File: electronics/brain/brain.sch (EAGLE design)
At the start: 7 parts

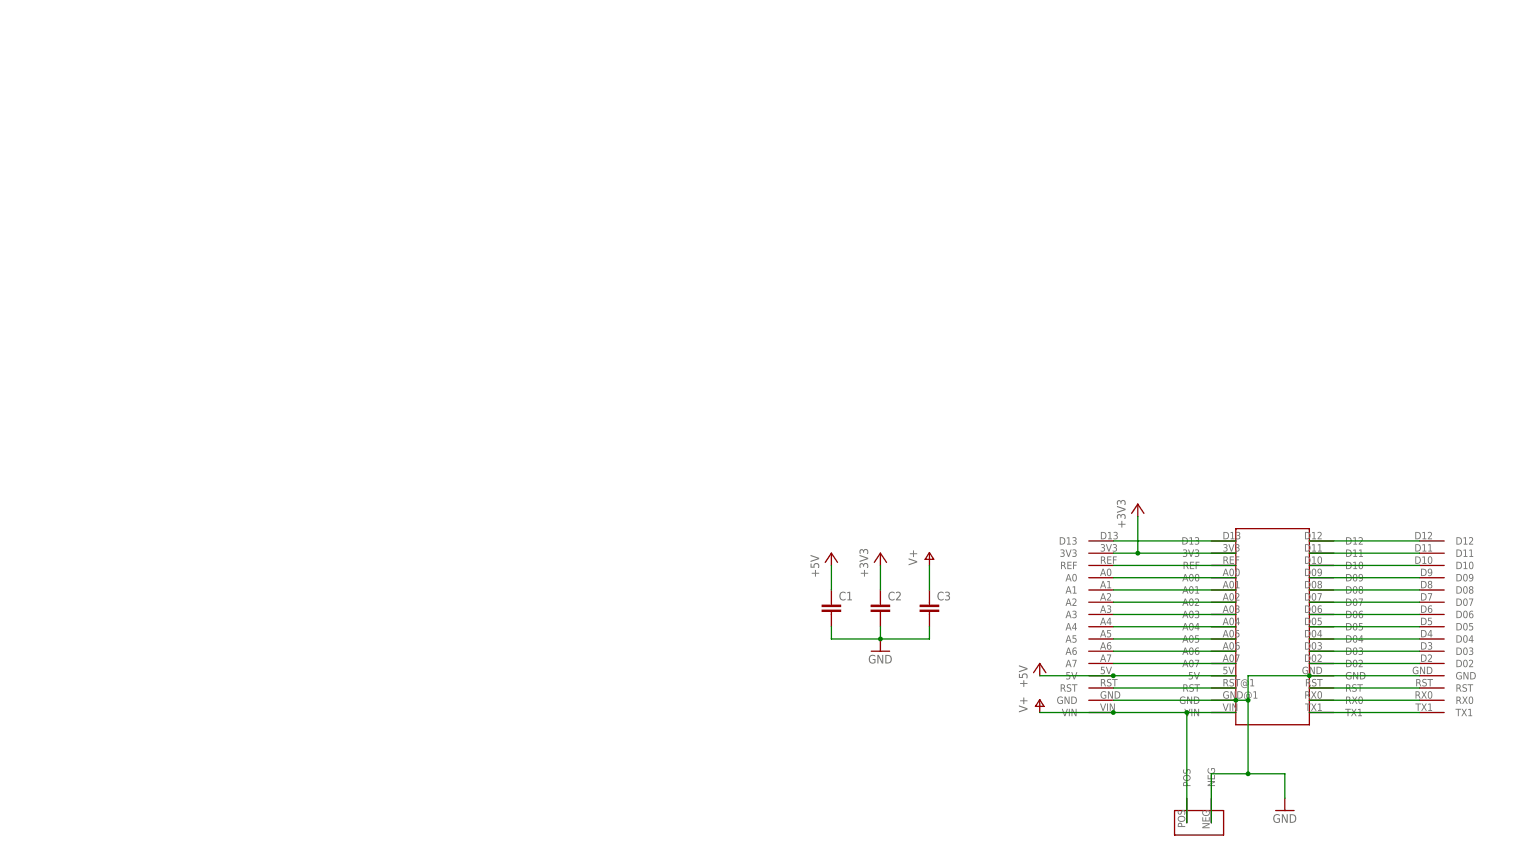
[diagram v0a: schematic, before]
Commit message: Fleshed out pin mapping. Routed new brain board.
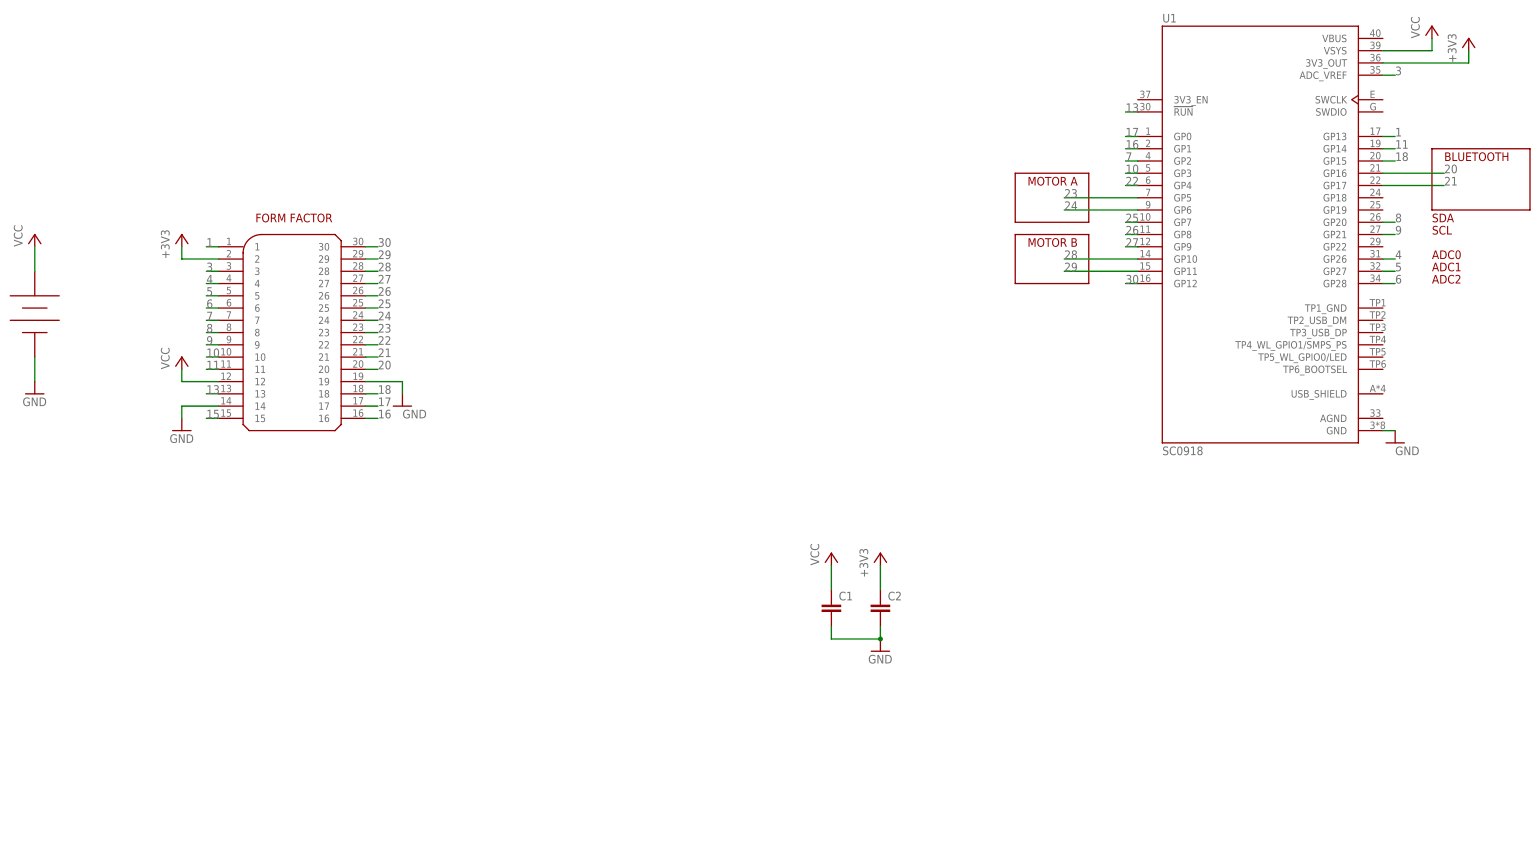
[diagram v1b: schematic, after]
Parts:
- removed C3: (no value), rcl:C-EU050-025X075
- removed U$1: ARDUINO-NANO-V3, RC Car:ARDUINO-NANO-V3
- removed U$2: ARDUINO-NANO-JUMPER-1, RC Car:ARDUINO-NANO-JUMPER-1
- removed U$3: POWER-IN, RC Car:POWER-IN
- removed U$5: ARDUINO-NANO-JUMPER-2, RC Car:ARDUINO-NANO-JUMPER-2
- added U$4: RC_FORM_FACTOR, rc_car:RC_FORM_FACTOR
- added U$6: LIPO_BATTERY, GIX:LIPO_BATTERY
- added U1: SC0918, SC0918:SC0918
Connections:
- removed net +5V: C1.1, U$1.5V, U$5.5V
- removed net A00: U$1.A00, U$5.A0
- removed net A01: U$1.A01, U$5.A1
- removed net A02: U$1.A02, U$5.A2
- removed net A03: U$1.A03, U$5.A3
- removed net A04: U$1.A04, U$5.A4
- removed net A05: U$1.A05, U$5.A5
- removed net A06: U$1.A06, U$5.A6
- removed net A07: U$1.A07, U$5.A7
- removed net D02: U$1.D02, U$2.D02
- removed net D03: U$1.D03, U$2.D03
- removed net D04: U$1.D04, U$2.D04
- removed net D05: U$1.D05, U$2.D05
- removed net D06: U$1.D06, U$2.D06
- removed net D07: U$1.D07, U$2.D07
- removed net D08: U$1.D08, U$2.D08
- removed net D09: U$1.D09, U$2.D09
- removed net D10: U$1.D10, U$2.D10
- removed net D11: U$1.D11, U$2.D11
- removed net D12: U$1.D12, U$2.D12
- removed net D13: U$1.D13, U$5.D13
- removed net REF: U$1.REF, U$5.REF
- removed net RST: U$1.RST, U$1.RST@1, U$2.RST, U$5.RST
- removed net RX0: U$1.RX0, U$2.RX0
- removed net TX1: U$1.TX1, U$2.TX1
- removed net V+: C3.1, U$1.VIN, U$3.POS, U$5.VIN
- new net 1: U$4.1, U1.GP13
- new net 10: U$4.10, U1.GP3
- new net 11: U$4.11, U1.GP14
- new net 13: U$4.13, U1.!RUN
- new net 15: U$4.15
- new net 16: U$4.16, U1.GP1
- new net 17: U$4.17, U1.GP0
- new net 18: U$4.18, U1.GP15
- new net 20: U$4.20, U1.GP16
- new net 21: U$4.21, U1.GP17
- new net 22: U$4.22, U1.GP4
- new net 23: U$4.23, U1.GP5
- new net 24: U$4.24, U1.GP6
- new net 25: U$4.25, U1.GP7
- new net 26: U$4.26, U1.GP8
- new net 27: U$4.27, U1.GP9
- new net 28: U$4.28, U1.GP10
- new net 29: U$4.29, U1.GP11
- new net 3: U$4.3, U1.ADC_VREF
- new net 30: U$4.30, U1.GP12
- new net 4: U$4.4, U1.GP26
- new net 5: U$4.5, U1.GP27
- new net 6: U$4.6, U1.GP28
- new net 7: U$4.7, U1.GP2
- new net 8: U$4.8, U1.GP20
- new net 9: U$4.9, U1.GP21
- new net VCC: C1.1, U$4.12, U$6.POS, U1.VSYS
- net +3V3: now also U$4.2, U1.3V3_OUT; no longer U$1.3V3, U$5.3V3
- net GND: now also U$4.14, U$4.19, U$6.NEG, U1.GND; no longer C3.2, U$1.GND, U$1.GND@1, U$2.GND, U$3.NEG, U$5.GND
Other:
- note added: "ADC0"
- note added: "ADC1"
- note added: "ADC2"
- note added: "BLUETOOTH"
- note added: "FORM FACTOR"
- note added: "MOTOR A"
- note added: "MOTOR B"
- note added: "SCL"
- note added: "SDA"

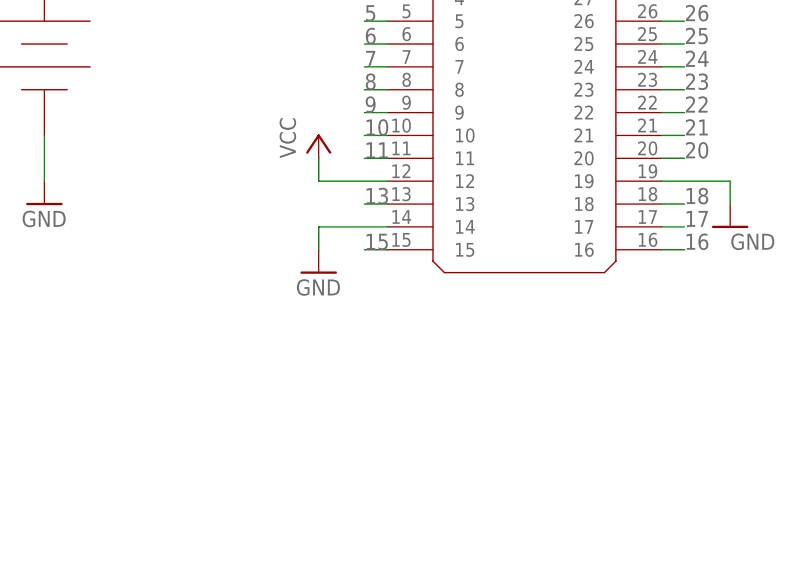
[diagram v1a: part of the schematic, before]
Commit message: Fixed power issue in current iteration of boards.
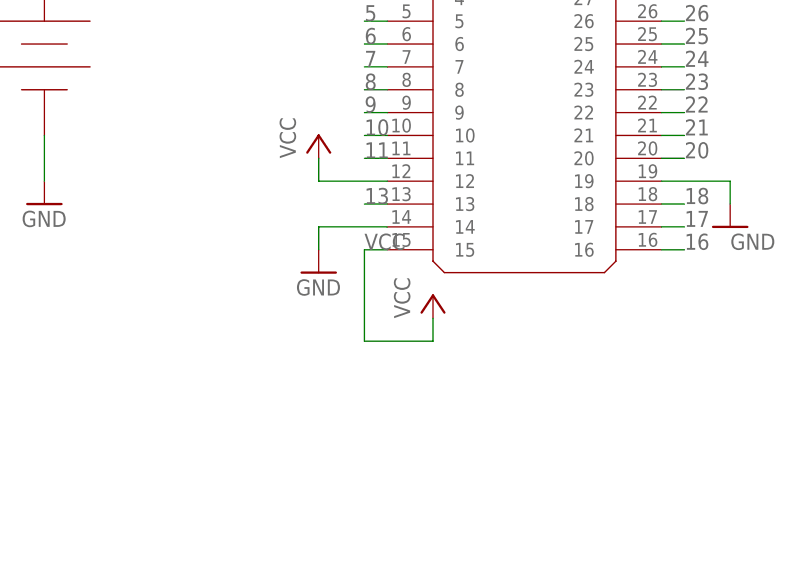
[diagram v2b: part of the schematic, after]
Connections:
- removed net 15: U$4.15
- net VCC: now also U$4.15
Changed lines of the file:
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@@
 <part name="GND6" library="supply1" library_urn="urn:adsk.eagle:library:371" deviceset="GND" device=""/>
 <part name="P+1" library="supply1" library_urn="urn:adsk.eagle:library:371" deviceset="VCC" device=""/>
+<part name="P+2" library="supply1" library_urn="urn:adsk.eagle:library:371" deviceset="VCC" device=""/>
 </parts>
 <sheets>
@@
 <attribute name="VALUE" x="-88.9" y="20.32" size="1.778" layer="96" rot="R90"/>
 </instance>
+<instance part="P+2" gate="VCC" x="-208.28" y="45.72" smashed="yes">
+<attribute name="VALUE" x="-210.82" y="43.18" size="1.778" layer="96" rot="R90"/>
+</instance>
 </instances>
 <busses>
@@
 <pinref part="P+1" gate="VCC" pin="VCC"/>
 </segment>
+<segment>
+<pinref part="U$4" gate="G$1" pin="15"/>
+<wire x1="-213.36" y1="50.8" x2="-215.9" y2="50.8" width="0.1524" layer="91"/>
+<label x="-215.9" y="50.8" size="1.778" layer="95"/>
+<wire x1="-215.9" y1="50.8" x2="-215.9" y2="40.64" width="0.1524" layer="91"/>
+<wire x1="-215.9" y1="40.64" x2="-208.28" y2="40.64" width="0.1524" layer="91"/>
+<pinref part="P+2" gate="VCC" pin="VCC"/>
+<wire x1="-208.28" y1="40.64" x2="-208.28" y2="43.18" width="0.1524" layer="91"/>
+</segment>
 </net>
 <net name="1" class="0">
@@
 </segment>
 </net>
-<net name="15" class="0">
-<segment>
-<pinref part="U$4" gate="G$1" pin="15"/>
-<wire x1="-213.36" y1="50.8" x2="-215.9" y2="50.8" width="0.1524" layer="91"/>
-<label x="-215.9" y="50.8" size="1.778" layer="95"/>
-</segment>
-</net>
